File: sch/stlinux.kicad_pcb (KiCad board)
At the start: 4 copper layers, 59 x 29 mm, 73 parts, among them J301 Micro_SD_Card_Det, J401 Extension, J501 USB_B_Mini, SW401 RESET_Sw, SW402 USER_Sw, U201 STM32F446ZCTx, U301 24LC08, U302 IS25LP064A-JBLE, U303 IS42S16160B-7TL, U501 FT230XS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

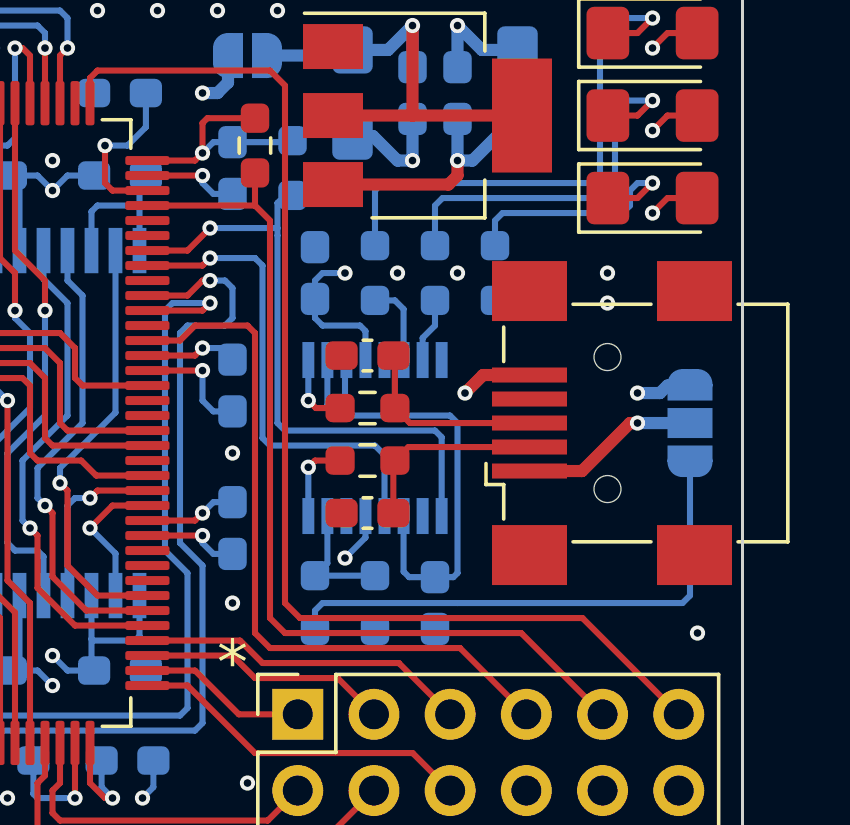
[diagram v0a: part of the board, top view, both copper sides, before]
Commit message: Replaced FTDI package with QFN one
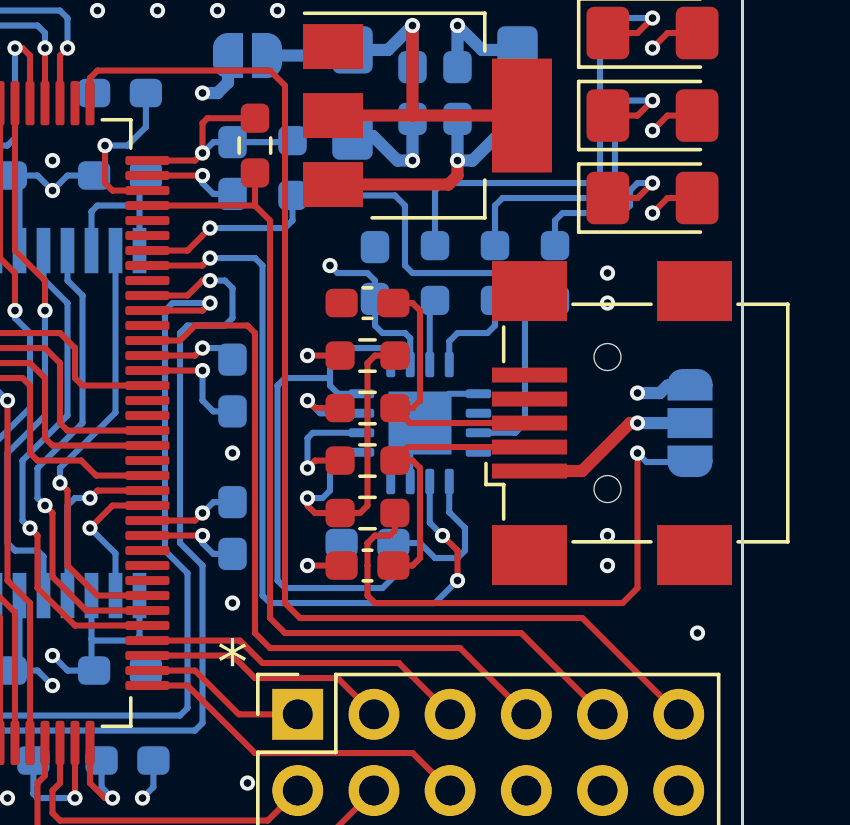
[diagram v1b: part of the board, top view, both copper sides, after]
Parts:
- R501, R502: moved to F.Cu
- U501: value FT230XS -> FT230XQ; footprint Package_SO:SSOP-16_3.9x4.9mm_P0.635mm -> Package_DFN_QFN:QFN-16-1EP_4x4mm_P0.65mm_EP2.1x2.1mm
- moved R502 8.25 mm to (164.0, 94.8), turned to 180 degrees
- moved R501 3.47 mm to (164.0, 100.0), turned to 0 degrees
- moved C503 3.01 mm to (164.0, 101.0), turned to 180 degrees
- moved C504 2.00 mm to (164.2, 92.0)
- moved R506 2.00 mm to (168.2, 92.0)
- moved R507 2.00 mm to (166.2, 92.0)
- moved R601 2.00 mm to (170.2, 92.0)
- moved C501 1.75 mm to (164.0, 101.8)
- moved C502 1.75 mm to (164.0, 93.0)
- moved U501 1.58 mm to (165.8, 97.0)
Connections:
- U501 pad 1: /MCU/UART1.RX -> Net-(C503-Pad1)
- U501 pad 10: Net-(C503-Pad1) -> VDD
- U501 pad 11: Net-(C503-Pad1) -> Net-(R507-Pad1)
- U501 pad 12: VDD -> Net-(R506-Pad1)
- U501 pad 14: Net-(R507-Pad1) -> unconnected-(U501-Pad14)
- U501 pad 15: Net-(R506-Pad1) -> /MCU/UART1.RX
- U501 pad 2: unconnected-(U501-Pad2) -> /MCU/UART1.TX
- U501 pad 3: Net-(C503-Pad1) -> GND
- U501 pad 4: /MCU/UART1.TX -> unconnected-(U501-Pad4)
- U501 pad 5: GND -> /UART/VSENSE
- U501 pad 6: unconnected-(U501-Pad6) -> Net-(R504-Pad2)
- U501 pad 7: /UART/VSENSE -> Net-(R503-Pad2)
- U501 pad 8: Net-(R504-Pad2) -> Net-(C503-Pad1)
- U501 pad 9: Net-(R503-Pad2) -> Net-(C503-Pad1)
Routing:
- net /MCU/UART1.TX: track 16.1 -> 25.6 mm, vias 1 -> 3
- net /UART/VSENSE: track 4.16 -> 11.2 mm, vias 0 -> 1
- net Net-(C503-Pad1): track 16.7 -> 23.5 mm
- net Net-(C502-Pad1): track 6.47 -> 9.63 mm
- net Net-(C501-Pad1): track 6.44 -> 9.61 mm
- net GND: track 98.5 -> 101.1 mm
- net Net-(D502-Pad1): track 18.1 -> 16.1 mm
- net Net-(D601-Pad1): track 8.59 -> 6.59 mm
- net Net-(D501-Pad1): track 13.3 -> 11.3 mm
- net /MCU/UART1.RX: track 21.0 -> 22.6 mm
- net Net-(JP501-Pad3): track 17.8 -> 19.1 mm, vias 0 -> 1
- net Net-(R504-Pad2): track 2.78 -> 4.06 mm
- net Net-(R506-Pad1): track 2.16 -> 3.35 mm
- net Net-(R503-Pad2): track 2.51 -> 3.17 mm
- net Net-(R507-Pad1): track 2.77 -> 2.21 mm

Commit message: Added OSHW logo on the board
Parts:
- added REF**: OSHW-Logo_5.7x6mm_SilkScreen, Symbol:OSHW-Logo_5.7x6mm_SilkScreen, B.Cu at (170.8, 102.8)

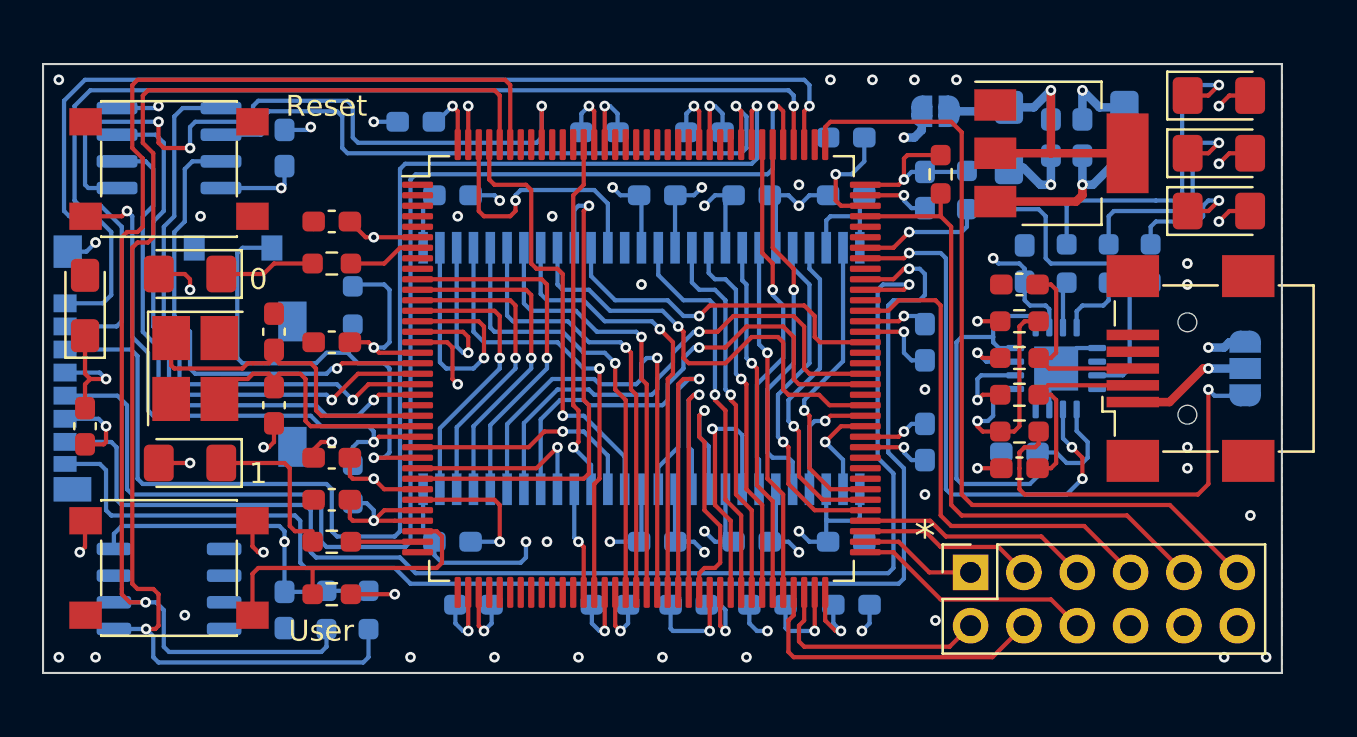
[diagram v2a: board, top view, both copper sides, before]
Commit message: Added more expansion capability.
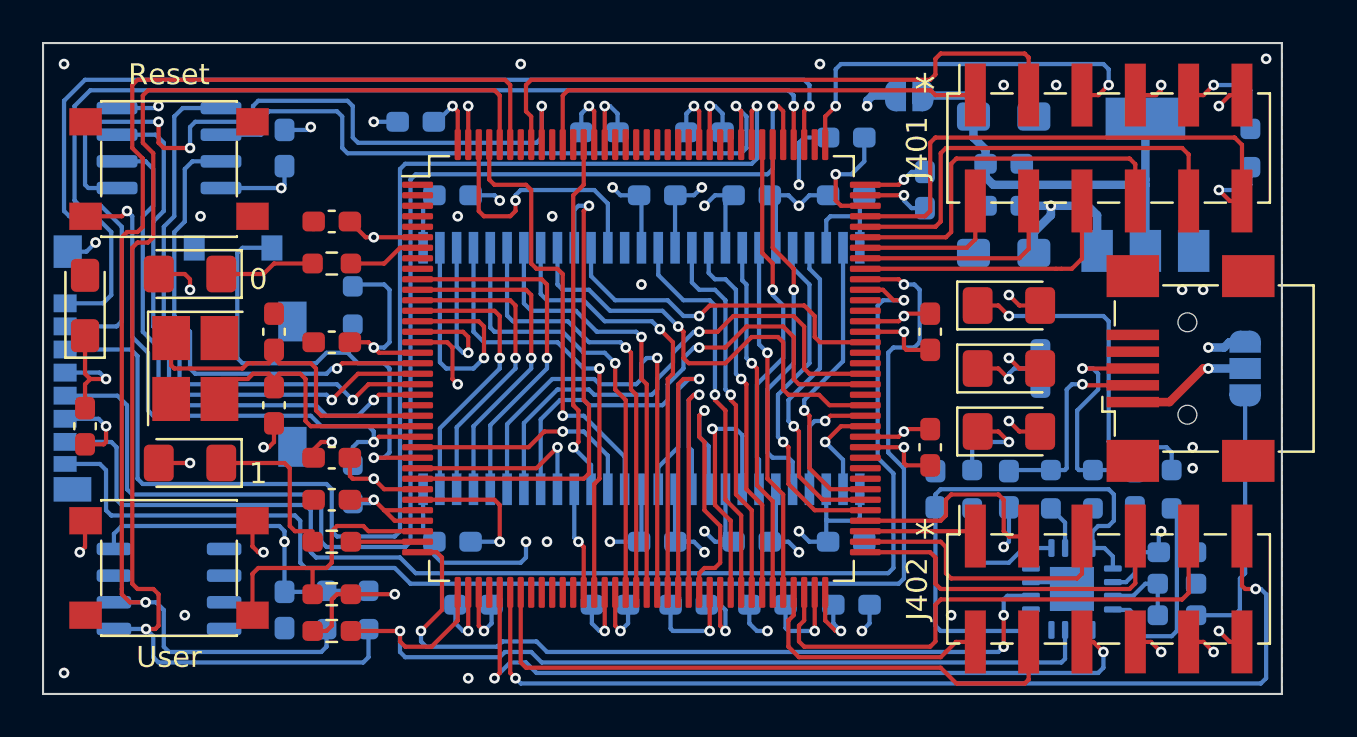
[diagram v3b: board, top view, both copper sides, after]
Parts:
- added J402: Extension, Connector_PinSocket_2.54mm:PinSocket_2x06_P2.54mm_Vertical_SMD, F.Cu at (168.2, 107.5)
- C210, C211, R505: moved to F.Cu
- C501, C502, R401, R501, R502, R503, R504, U601: moved to B.Cu
- J401: footprint Connector_PinSocket_2.54mm:PinSocket_2x06_P2.54mm_Vertical -> Connector_PinSocket_2.54mm:PinSocket_2x06_P2.54mm_Vertical_SMD
- U303: value IS42S16160B-7TL -> IS42S16160J
- moved R505 36.8 mm to (131.2, 109.5), turned to 180 degrees
- moved J401 21.3 mm to (168.2, 86.5)
- moved D502 18.9 mm to (163.5, 100.0)
- moved C504 15.5 mm to (171.5, 105.8), turned to 0 degrees
- moved R401 14.8 mm to (175.0, 86.5)
- moved R502 14.6 mm to (171.5, 107.2), turned to 0 degrees
- moved D601 12.5 mm to (163.5, 97.0)
- moved D501 12.4 mm to (163.5, 94.0)
- moved R507 11.7 mm to (161.8, 102.8)
- moved R501 11.5 mm to (171.5, 108.8)
- moved REF** 11.4 mm to (161.0, 96.8), turned to 180 degrees
- moved C502 11.2 mm to (169.5, 102.8), turned to -90 degrees
- moved R506 11.2 mm to (171.2, 102.8)
- moved U501 10.5 mm to (166.5, 107.5), turned to 0 degrees
- moved C601 7.96 mm to (163.2, 91.5), turned to 180 degrees
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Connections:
- J401 pad 1: /Low level IO/EXT.PB13 -> /Low level IO/EXT.PB4
- J401 pad 10: VDD -> /Low level IO/EXT.PA12
- J401 pad 11: /Low level IO/SWD.CLK -> +5V
- J401 pad 12: +5V -> /Low level IO/SWD.DIO
- J401 pad 2: /Low level IO/EXT.PB11 -> /Low level IO/EXT.PA10
- J401 pad 3: /Low level IO/EXT.PB14 -> /Low level IO/EXT.PB7
- J401 pad 4: /Low level IO/EXT.PB10 -> /Low level IO/EXT.PA9
- J401 pad 5: /Low level IO/EXT.PB15 -> /Low level IO/SWD.CLK
- J401 pad 6: /Low level IO/EXT.PB12 -> /Low level IO/EXT.PA8
- J401 pad 7: /Low level IO/EXT.PC6 -> GND
- J401 pad 8: GND -> /Low level IO/EXT.PA11
- J401 pad 9: /Low level IO/SWD.DIO -> VDD
- R505 pad 1: /MCU/UART1.RX -> /MCU/UART2.RX
- U201 pad 100: unconnected-(U201-Pad100) -> /Low level IO/EXT.PA8
- U201 pad 101: /MCU/UART1.TX -> /Low level IO/EXT.PA9
- U201 pad 102: /MCU/UART1.RX -> /Low level IO/EXT.PA10
- U201 pad 103: unconnected-(U201-Pad103) -> /Low level IO/EXT.PA11
- U201 pad 104: unconnected-(U201-Pad104) -> /Low level IO/EXT.PA12
- U201 pad 134: unconnected-(U201-Pad134) -> /Low level IO/EXT.PB4
- U201 pad 137: unconnected-(U201-Pad137) -> /Low level IO/EXT.PB7
- U201 pad 36: unconnected-(U201-Pad36) -> /MCU/UART2.TX
- U201 pad 37: unconnected-(U201-Pad37) -> /MCU/UART2.RX
- U201 pad 41: unconnected-(U201-Pad41) -> /Low level IO/EXT.PA5
- U201 pad 42: unconnected-(U201-Pad42) -> /Low level IO/EXT.PA6
- U201 pad 43: unconnected-(U201-Pad43) -> /Low level IO/EXT.PA7
- U201 pad 96: /Low level IO/EXT.PC6 -> unconnected-(U201-Pad96)
- U501 pad 11: Net-(R507-Pad1) -> /UART/VSENSE
- U501 pad 15: /MCU/UART1.RX -> /MCU/UART2.RX
- U501 pad 2: /MCU/UART1.TX -> /MCU/UART2.TX
- U501 pad 5: /UART/VSENSE -> Net-(R507-Pad1)
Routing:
- net /Low level IO/EXT.PA6: track 0.00 -> 47.8 mm, vias 0 -> 2
- net /MCU/UART2.RX: track 0.00 -> 41.8 mm, vias 0 -> 1
- net /MCU/UART2.TX: track 0.00 -> 37.6 mm, vias 0 -> 3
- net /Low level IO/EXT.PA5: track 0.00 -> 35.8 mm, vias 0 -> 2
- net /Low level IO/EXT.PA7: track 0.00 -> 29.8 mm
- net /Low level IO/EXT.PB7: track 0.00 -> 29.8 mm
- net /MCU/UART1.TX: track 25.6 -> 0.00 mm, vias 3 -> 0
- net /Low level IO/EXT.PC6: track 24.1 -> 0.00 mm
- net /MCU/UART1.RX: track 22.6 -> 0.00 mm, vias 1 -> 0
- net /Low level IO/EXT.PB4: track 0.00 -> 22.2 mm
- net /Low level IO/EXT.PA12: track 0.00 -> 21.2 mm
- net /Low level IO/SWD.CLK: track 39.6 -> 19.2 mm, vias 0 -> 2
- net /Low level IO/EXT.PA11: track 0.00 -> 18.2 mm
- net /Low level IO/EXT.PB11: track 11.1 -> 25.9 mm
- net /Low level IO/EXT.PA8: track 0.00 -> 13.3 mm
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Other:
- board size 59 x 29 mm -> 59 x 31 mm
- board text added: "December 2022"
- board text removed: "November 2022"

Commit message: Add JLCPCB order ID placeholder under IC
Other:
- board text added: "JLCJLCJLCJLC"
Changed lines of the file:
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@@
     (solder_mask_min_width 0.1016)
     (pcbplotparams
-      (layerselection 0x00010fc_ffffffff)
+      (layerselection 0x00010f0_ffffffff)
       (disableapertmacros false)
-      (usegerberextensions false)
-      (usegerberattributes true)
-      (usegerberadvancedattributes true)
-      (creategerberjobfile true)
+      (usegerberextensions true)
+      (usegerberattributes false)
+      (usegerberadvancedattributes false)
+      (creategerberjobfile false)
       (svguseinch false)
       (svgprecision 6)
@@
       (psa4output false)
       (plotreference true)
-      (plotvalue true)
+      (plotvalue false)
       (plotinvisibletext false)
       (sketchpadsonfab false)
-      (subtractmaskfromsilk false)
+      (subtractmaskfromsilk true)
       (outputformat 1)
       (mirror false)
-      (drillshape 1)
+      (drillshape 0)
       (scaleselection 1)
-      (outputdirectory "")
+      (outputdirectory "../ger/")
     )
   )
@@
     (fp_line (start -1.6 -0.4) (end -1.6 0.8) (layer "F.Fab") (width 0.1))
     (fp_line (start -1.2 -0.8) (end -1.6 -0.4) (layer "F.Fab") (width 0.1))
-    (pad "1" smd roundrect (at -1.4875 0 180) (size 1.425 1.75) (layers "F.Cu" "F.Paste" "F.Mask") (roundrect_rratio 0.175439)
+    (pad "1" smd roundrect (at -1.4875 0 180) (size 1.425 1.75) (layers "F.Cu" "F.Paste" "F.Mask") (roundrect_rratio 0.1754392982)
       (net 70 "Net-(D402-Pad1)") (pinfunction "K") (pintype "passive"))
-    (pad "2" smd roundrect (at 1.4875 0 180) (size 1.425 1.75) (layers "F.Cu" "F.Paste" "F.Mask") (roundrect_rratio 0.175439)
+    (pad "2" smd roundrect (at 1.4875 0 180) (size 1.425 1.75) (layers "F.Cu" "F.Paste" "F.Mask") (roundrect_rratio 0.1754392982)
       (net 2 "VDD") (pinfunction "A") (pintype "passive"))
     (model "${KICAD6_3DMODEL_DIR}/LED_SMD.3dshapes/LED_1206_3216Metric.wrl"
@@
     (fp_line (start -1.2 -0.8) (end -1.6 -0.4) (layer "F.Fab") (width 0.1))
     (fp_line (start 1.6 -0.8) (end -1.2 -0.8) (layer "F.Fab") (width 0.1))
-    (pad "1" smd roundrect (at -1.4875 0) (size 1.425 1.75) (layers "F.Cu" "F.Paste" "F.Mask") (roundrect_rratio 0.175439)
+    (pad "1" smd roundrect (at -1.4875 0) (size 1.425 1.75) (layers "F.Cu" "F.Paste" "F.Mask") (roundrect_rratio 0.1754392982)
       (net 133 "Net-(D601-Pad1)") (pinfunction "K") (pintype "passive"))
-    (pad "2" smd roundrect (at 1.4875 0) (size 1.425 1.75) (layers "F.Cu" "F.Paste" "F.Mask") (roundrect_rratio 0.175439)
+    (pad "2" smd roundrect (at 1.4875 0) (size 1.425 1.75) (layers "F.Cu" "F.Paste" "F.Mask") (roundrect_rratio 0.1754392982)
       (net 2 "VDD") (pinfunction "A") (pintype "passive"))
     (model "${KICAD6_3DMODEL_DIR}/LED_SMD.3dshapes/LED_1206_3216Metric.wrl"
@@
     (fp_line (start 1.6 0.8) (end 1.6 -0.8) (layer "F.Fab") (width 0.1))
     (fp_line (start -1.6 -0.4) (end -1.6 0.8) (layer "F.Fab") (width 0.1))
-    (pad "1" smd roundrect (at -1.4875 0 180) (size 1.425 1.75) (layers "F.Cu" "F.Paste" "F.Mask") (roundrect_rratio 0.175439)
+    (pad "1" smd roundrect (at -1.4875 0 180) (size 1.425 1.75) (layers "F.Cu" "F.Paste" "F.Mask") (roundrect_rratio 0.1754392982)
       (net 69 "Net-(D401-Pad1)") (pinfunction "K") (pintype "passive"))
-    (pad "2" smd roundrect (at 1.4875 0 180) (size 1.425 1.75) (layers "F.Cu" "F.Paste" "F.Mask") (roundrect_rratio 0.175439)
+    (pad "2" smd roundrect (at 1.4875 0 180) (size 1.425 1.75) (layers "F.Cu" "F.Paste" "F.Mask") (roundrect_rratio 0.1754392982)
       (net 2 "VDD") (pinfunction "A") (pintype "passive"))
     (model "${KICAD6_3DMODEL_DIR}/LED_SMD.3dshapes/LED_1206_3216Metric.wrl"
@@
     (fp_line (start 1.6 -0.8) (end -1.2 -0.8) (layer "F.Fab") (width 0.1))
     (fp_line (start 1.6 0.8) (end 1.6 -0.8) (layer "F.Fab") (width 0.1))
-    (pad "1" smd roundrect (at -1.4375 0 90) (size 1.575 1.35) (layers "F.Cu" "F.Paste" "F.Mask") (roundrect_rratio 0.185185)
+    (pad "1" smd roundrect (at -1.4375 0 90) (size 1.575 1.35) (layers "F.Cu" "F.Paste" "F.Mask") (roundrect_rratio 0.1851851852)
       (net 2 "VDD") (pintype "passive"))
-    (pad "2" smd roundrect (at 1.4375 0 90) (size 1.575 1.35) (layers "F.Cu" "F.Paste" "F.Mask") (roundrect_rratio 0.185185)
+    (pad "2" smd roundrect (at 1.4375 0 90) (size 1.575 1.35) (layers "F.Cu" "F.Paste" "F.Mask") (roundrect_rratio 0.1851851852)
       (net 1 "GND") (pintype "passive"))
     (model "${KICAD6_3DMODEL_DIR}/Capacitor_Tantalum_SMD.3dshapes/CP_EIA-3216-18_Kemet-A.wrl"
@@
     (fp_line (start 1.6 0.8) (end 1.6 -0.8) (layer "F.Fab") (width 0.1))
     (fp_line (start -1.6 0.8) (end 1.6 0.8) (layer "F.Fab") (width 0.1))
-    (pad "1" smd roundrect (at -1.4875 0) (size 1.425 1.75) (layers "F.Cu" "F.Paste" "F.Mask") (roundrect_rratio 0.175439)
+    (pad "1" smd roundrect (at -1.4875 0) (size 1.425 1.75) (layers "F.Cu" "F.Paste" "F.Mask") (roundrect_rratio 0.1754392982)
       (net 118 "Net-(D501-Pad1)") (pinfunction "K") (pintype "passive"))
-    (pad "2" smd roundrect (at 1.4875 0) (size 1.425 1.75) (layers "F.Cu" "F.Paste" "F.Mask") (roundrect_rratio 0.175439)
+    (pad "2" smd roundrect (at 1.4875 0) (size 1.425 1.75) (layers "F.Cu" "F.Paste" "F.Mask") (roundrect_rratio 0.1754392982)
       (net 2 "VDD") (pinfunction "A") (pintype "passive"))
     (model "${KICAD6_3DMODEL_DIR}/LED_SMD.3dshapes/LED_1206_3216Metric.wrl"
@@
     (fp_line (start -1.6 -0.4) (end -1.6 0.8) (layer "F.Fab") (width 0.1))
     (fp_line (start -1.2 -0.8) (end -1.6 -0.4) (layer "F.Fab") (width 0.1))
-    (pad "1" smd roundrect (at -1.4875 0) (size 1.425 1.75) (layers "F.Cu" "F.Paste" "F.Mask") (roundrect_rratio 0.175439)
+    (pad "1" smd roundrect (at -1.4875 0) (size 1.425 1.75) (layers "F.Cu" "F.Paste" "F.Mask") (roundrect_rratio 0.1754392982)
       (net 119 "Net-(D502-Pad1)") (pinfunction "K") (pintype "passive"))
-    (pad "2" smd roundrect (at 1.4875 0) (size 1.425 1.75) (layers "F.Cu" "F.Paste" "F.Mask") (roundrect_rratio 0.175439)
+    (pad "2" smd roundrect (at 1.4875 0) (size 1.425 1.75) (layers "F.Cu" "F.Paste" "F.Mask") (roundrect_rratio 0.1754392982)
       (net 2 "VDD") (pinfunction "A") (pintype "passive"))
     (model "${KICAD6_3DMODEL_DIR}/LED_SMD.3dshapes/LED_1206_3216Metric.wrl"
@@
     (fp_line (start 1.6 -0.8) (end 1.6 0.8) (layer "B.Fab") (width 0.1))
     (fp_line (start -1.6 -0.8) (end 1.6 -0.8) (layer "B.Fab") (width 0.1))
-    (pad "1" smd roundrect (at -1.4375 0) (size 1.575 1.35) (layers "B.Cu" "B.Paste" "B.Mask") (roundrect_rratio 0.185185)
+    (pad "1" smd roundrect (at -1.4375 0) (size 1.575 1.35) (layers "B.Cu" "B.Paste" "B.Mask") (roundrect_rratio 0.1851851852)
       (net 132 "/Power/+3V3") (pintype "passive"))
-    (pad "2" smd roundrect (at 1.4375 0) (size 1.575 1.35) (layers "B.Cu" "B.Paste" "B.Mask") (roundrect_rratio 0.185185)
+    (pad "2" smd roundrect (at 1.4375 0) (size 1.575 1.35) (layers "B.Cu" "B.Paste" "B.Mask") (roundrect_rratio 0.1851851852)
       (net 1 "GND") (pintype "passive"))
     (model "${KICAD6_3DMODEL_DIR}/Capacitor_Tantalum_SMD.3dshapes/CP_EIA-3216-18_Kemet-A.wrl"
@@
     (fp_line (start 1.6 -0.8) (end 1.6 0.8) (layer "B.Fab") (width 0.1))
     (fp_line (start -1.6 0.4) (end -1.6 -0.8) (layer "B.Fab") (width 0.1))
-    (pad "1" smd roundrect (at -1.4375 0 180) (size 1.575 1.35) (layers "B.Cu" "B.Paste" "B.Mask") (roundrect_rratio 0.185185)
+    (pad "1" smd roundrect (at -1.4375 0 180) (size 1.575 1.35) (layers "B.Cu" "B.Paste" "B.Mask") (roundrect_rratio 0.1851851852)
       (net 124 "+5V") (pintype "passive"))
-    (pad "2" smd roundrect (at 1.4375 0 180) (size 1.575 1.35) (layers "B.Cu" "B.Paste" "B.Mask") (roundrect_rratio 0.185185)
+    (pad "2" smd roundrect (at 1.4375 0 180) (size 1.575 1.35) (layers "B.Cu" "B.Paste" "B.Mask") (roundrect_rratio 0.1851851852)
       (net 1 "GND") (pintype "passive"))
     (model "${KICAD6_3DMODEL_DIR}/Capacitor_Tantalum_SMD.3dshapes/CP_EIA-3216-18_Kemet-A.wrl"
@@
     (effects (font (size 0.8 0.8) (thickness 0.15)) (justify mirror))
   )
+  (gr_text "JLCJLCJLCJLC" (at 146 91.5) (layer "F.SilkS")
+    (effects (font (size 1.5 1.5) (thickness 0.3)))
+  )
   (gr_text "1" (at 127.75 102) (layer "F.SilkS")
     (effects (font (size 1 1) (thickness 0.15)))
@@
     (pts (xy 117.5 82) (xy 117.5 112))
     (height 3.5)
-    (gr_text "1181.1024 mils" (at 112.85 97 90) (layer "Cmts.User")
+    (gr_text "30 mm" (at 112.85 97 90) (layer "Cmts.User")
       (effects (font (size 1 1) (thickness 0.15)))
     )
@@
     (pts (xy 117.5 82) (xy 176.5 82))
     (height -4.5)
-    (gr_text "2322.8346 mils" (at 147 76.35) (layer "Cmts.User")
+    (gr_text "59 mm" (at 147 76.35) (layer "Cmts.User")
       (effects (font (size 1 1) (thickness 0.15)))
     )
